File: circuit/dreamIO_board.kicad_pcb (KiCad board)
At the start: 2 copper layers, 60 x 60 mm, 82 parts, among them IC1 TPS61200, P1 BATT, P2 CONN_01X08, P3 CONN_01X08, P4 CONN_01X02, P5 CONN_01X06, P6 gnd_con, P7 CONN_01X03, P8 NO_CASCADE, P9 PixelOut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

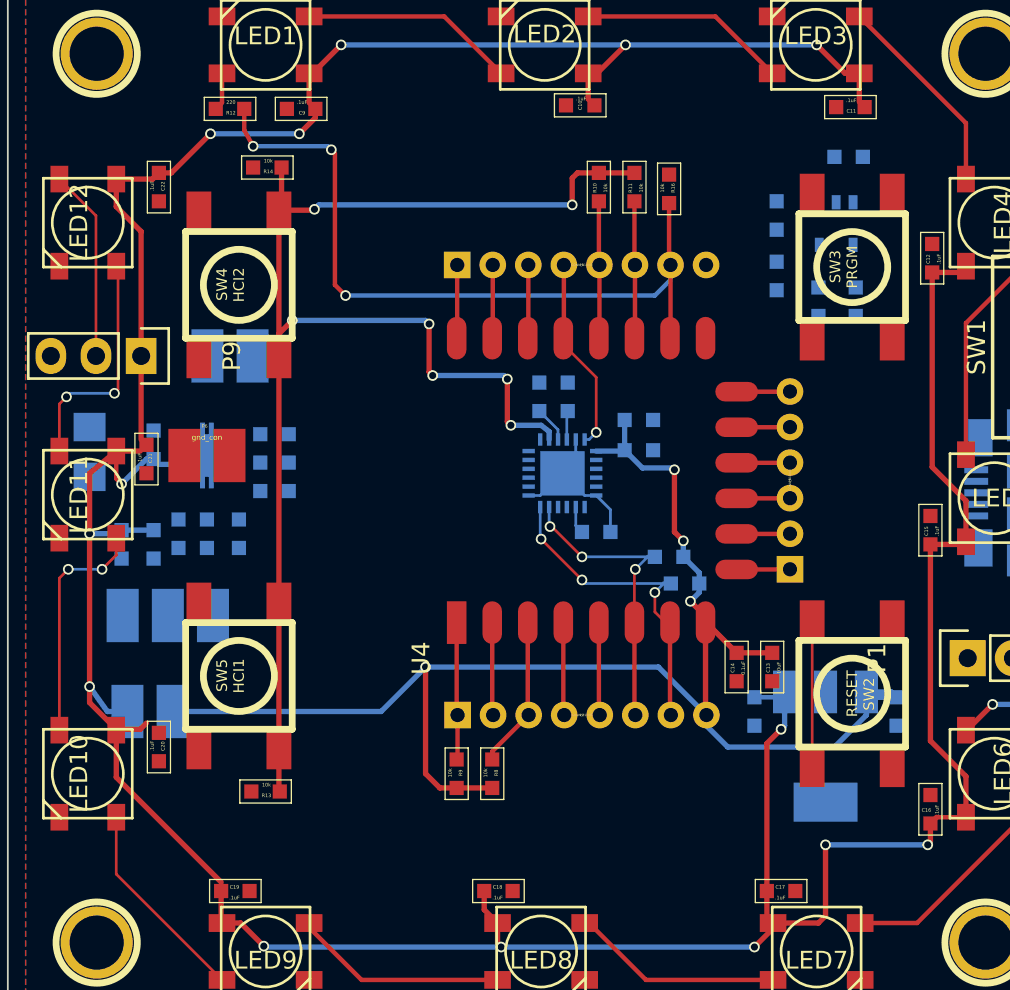
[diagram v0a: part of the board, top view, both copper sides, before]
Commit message: removed the 3.3V regulator. The TPS61200 is now the main regulator and will be 5V.
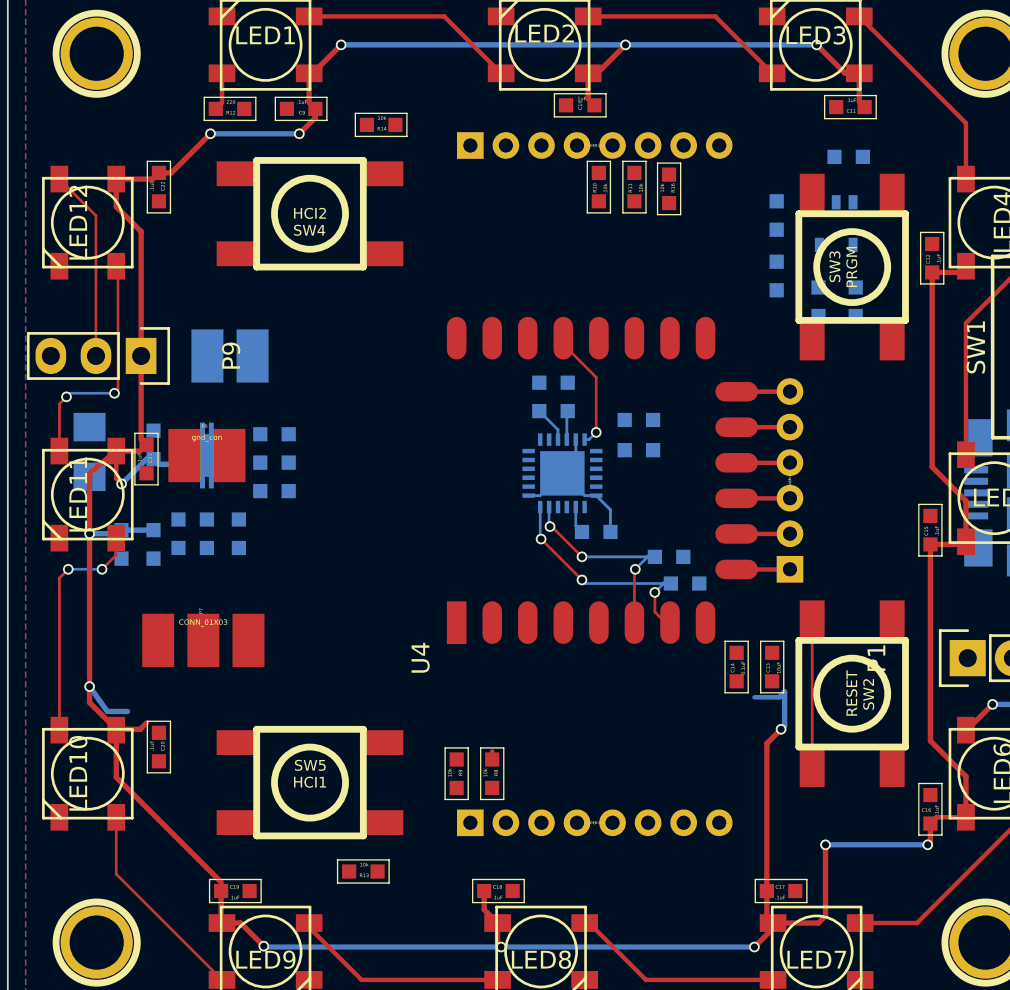
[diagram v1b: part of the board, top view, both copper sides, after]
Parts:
- removed C7: .33uF, kicad-libraries:0603
- removed C8: .1uF, kicad-libraries:0603
- removed P8: NO_CASCADE, _connectors:_Solder_Pad2.54_2
- removed U3: UA78M33_SOT223, kicad-libraries:SOT-223
- P7: moved to F.Cu
- moved SW5 7.21 mm to (31.3, 59.7), turned to 0 degrees
- moved R13 7.11 mm to (34.3, 64.7)
- moved R14 6.84 mm to (35.3, 22.7)
- moved P3 6.76 mm to (47.3, 23.9)
- moved P2 6.10 mm to (47.3, 62.0)
- moved SW4 5.66 mm to (31.3, 27.7), turned to 180 degrees
- moved P7 2.44 mm to (25.3, 51.7)
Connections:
- C10 pad 2: VCC -> +3V3
- C11 pad 2: VCC -> +3V3
- C12 pad 2: VCC -> +3V3
- C15 pad 2: VCC -> +3V3
- C16 pad 2: VCC -> +3V3
- C17 pad 2: VCC -> +3V3
- C18 pad 2: VCC -> +3V3
- C19 pad 2: VCC -> +3V3
- C20 pad 2: VCC -> +3V3
- C21 pad 2: VCC -> +3V3
- C22 pad 2: VCC -> +3V3
- C5 pad 1: VCC -> +3V3
- C9 pad 2: VCC -> +3V3
- IC1 pad 2: VCC -> +3V3
- LED1 pad 1: VCC -> +3V3
- LED10 pad 1: VCC -> +3V3
- LED11 pad 1: VCC -> +3V3
- LED12 pad 1: VCC -> +3V3
- LED2 pad 1: VCC -> +3V3
- LED3 pad 1: VCC -> +3V3
- LED4 pad 1: VCC -> +3V3
- LED5 pad 1: VCC -> +3V3
- LED6 pad 1: VCC -> +3V3
- LED7 pad 1: VCC -> +3V3
- LED8 pad 1: VCC -> +3V3
- LED9 pad 1: VCC -> +3V3
- P9 pad 1: VCC -> (no net)
- R4 pad 1: VCC -> +3V3
- R5 pad 1: VCC -> +3V3
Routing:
- net VCC: track 220.3 -> 0.00 mm, vias 14 -> 0
- net +3V3: track 164.3 -> 220.3 mm, vias 11 -> 14
- net GPIO15: track 42.4 -> 0.04 mm, vias 3 -> 0
- net CH_PD: track 8.57 -> 0.45 mm
- net GPIO2: track 7.72 -> 0.04 mm
- net GPIO0: track 7.72 -> 0.04 mm
- net RESET: track 16.1 -> 8.47 mm
- net GPIO13: track 18.7 -> 13.5 mm
- net GPIO12: track 17.4 -> 12.1 mm
- net GPIO16: track 5.22 -> 0.00 mm
- net GPIO14: track 5.22 -> 0.00 mm
- net ADC: track 5.22 -> 0.00 mm
- net GPIO4: track 11.0 -> 6.92 mm
- net TX: track 4.13 -> 0.04 mm
- net RX: track 4.13 -> 0.04 mm
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
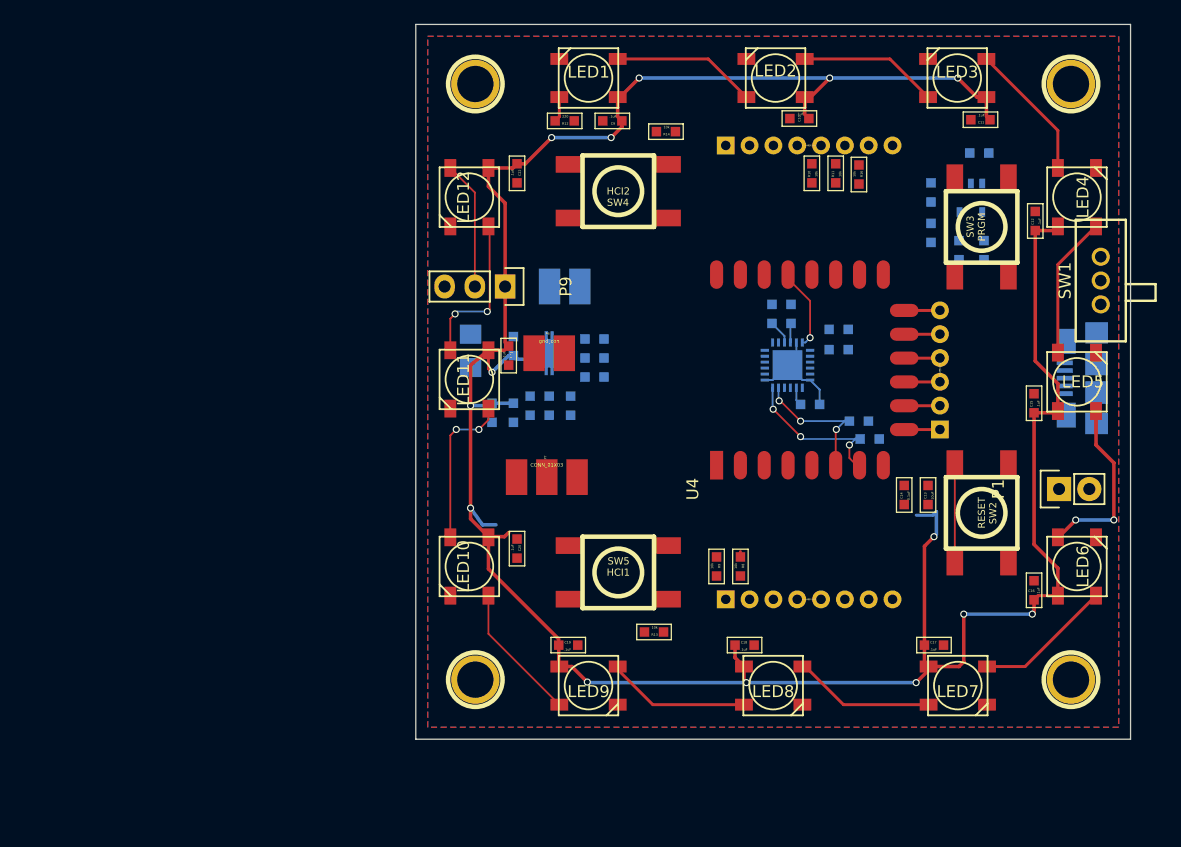
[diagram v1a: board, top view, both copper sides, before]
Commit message: added ADC voltage measurement. A voltage resistor of R1 2M and R2 330K keeps the maximum voltage of the battery (4.2V) below the 1V maximum for the analog pin. If the resistor network is not populated the pin remains empty
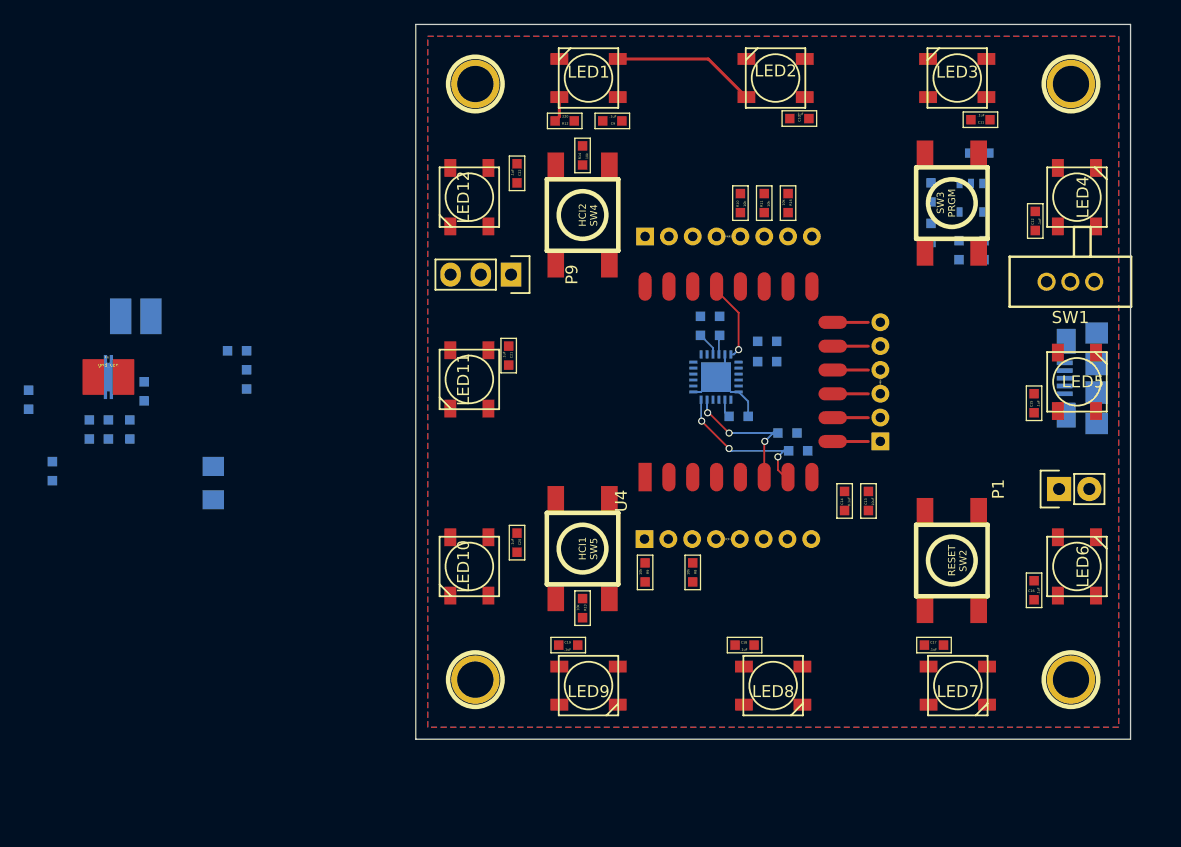
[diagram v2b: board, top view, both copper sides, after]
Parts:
- removed P7: CONN_01X03, _connectors:_Solder_Pad2.54_3
- removed R5: 2M, kicad-libraries:0603
- moved C5 40.9 mm to (-18.2, 45.2)
- moved R4 39.0 mm to (-16.2, 51.2)
- moved C3 37.1 mm to (-8.50, 44.5)
- moved C6 37.1 mm to (-13.1, 47.7)
- moved IC1 37.1 mm to (-11.5, 43.3)
- moved P6 37.1 mm to (-11.5, 43.3)
- moved R6 37.1 mm to (-11.5, 47.7)
- moved R7 37.1 mm to (-9.70, 47.7)
- moved P4 36.1 mm to (-9.20, 38.2)
- moved C4 30.0 mm to (0.10, 43.5)
- moved R3 30.0 mm to (-0.70, 41.1)
- moved L1 24.3 mm to (-2.70, 52.2)
- moved P3 10.2 mm to (40.5, 31.5)
- moved P2 8.49 mm to (40.5, 56.9)
- moved R14 7.28 mm to (28.3, 24.7), turned to 270 degrees
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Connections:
- R4 pad 2: Net-(P7-Pad3) -> Net-(IC1-Pad10)
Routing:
- net +3V3: track 220.3 -> 0.00 mm, vias 14 -> 0
- net Net-(LED5-Pad2): track 15.1 -> 0.05 mm, vias 2 -> 0
- net Net-(LED11-Pad2): track 13.3 -> 0.00 mm, vias 2 -> 0
- net Net-(LED10-Pad2): track 13.2 -> 0.00 mm, vias 2 -> 0
- net Net-(LED8-Pad2): track 12.1 -> 0.00 mm
- net Net-(LED7-Pad2): track 11.9 -> 0.00 mm
- net Net-(LED4-Pad2): track 11.9 -> 0.00 mm
- net Net-(LED2-Pad2): track 11.7 -> 0.00 mm
- net Net-(LED3-Pad2): track 11.6 -> 0.00 mm
- net Net-(LED6-Pad2): track 11.6 -> 0.00 mm
- net Net-(LED10-Pad4): track 11.6 -> 0.00 mm
- net DOUT: track 10.8 -> 0.00 mm
- net RESET: track 8.47 -> 0.00 mm

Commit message: changed position of on-off switch, batt connection, and USB input. Realized the USB plug didn`t have to be right in the center of one side
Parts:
- added R15: 330K, kicad-libraries:0603, F.Cu at (21.7, 79.3)
- added R5: 2M, kicad-libraries:0603, F.Cu at (23.3, 79.3)
- moved R4 79.3 mm to (63.1, 49.3), turned to 90 degrees
- moved R6 76.7 mm to (65.2, 47.7), turned to 180 degrees
- moved C5 75.6 mm to (57.4, 47.3), turned to 180 degrees
- moved IC1 73.0 mm to (61.5, 45.6)
- moved P6 73.0 mm to (61.5, 45.6), turned to 180 degrees
- moved C6 70.5 mm to (57.4, 48.8), turned to 180 degrees
- moved C3 68.4 mm to (59.9, 42.1), turned to 0 degrees
- moved P4 68.3 mm to (59.1, 39.1)
- moved R7 67.2 mm to (57.4, 50.3), turned to 180 degrees
- moved R3 66.1 mm to (65.2, 46.4), turned to 0 degrees
- moved C4 65.1 mm to (65.2, 44.8), turned to 180 degrees
- moved L1 60.4 mm to (57.1, 43.9), turned to 90 degrees
- moved SW1 18.2 mm to (68.1, 53.5)
- moved P1 3.06 mm to (68.9, 49.7)
- moved U2 2.31 mm to (73.1, 41.1)
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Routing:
- net RESET: track 0.00 -> 7.24 mm
- net CH_PD: track 0.00 -> 7.24 mm
- net GPIO2: track 0.04 -> 6.24 mm
- net GPIO15: track 0.04 -> 6.24 mm
- net GPIO0: track 0.04 -> 6.24 mm
- net GPIO16: track 0.00 -> 5.22 mm
- net GPIO14: track 0.00 -> 5.22 mm
- net GPIO13: track 13.5 -> 18.7 mm
- net ADC: track 0.00 -> 5.22 mm
- net +3V3: track 0.00 -> 5.22 mm
- net GPIO12: track 12.1 -> 17.4 mm
- net GPIO4: track 6.92 -> 11.1 mm
- net TX: track 0.04 -> 4.24 mm
- net RX: track 0.04 -> 4.24 mm
- net GPIO5: track 0.04 -> 4.24 mm
- added copper zone on B.Cu, net GNDA
- added copper zone on F.Cu, net GNDA

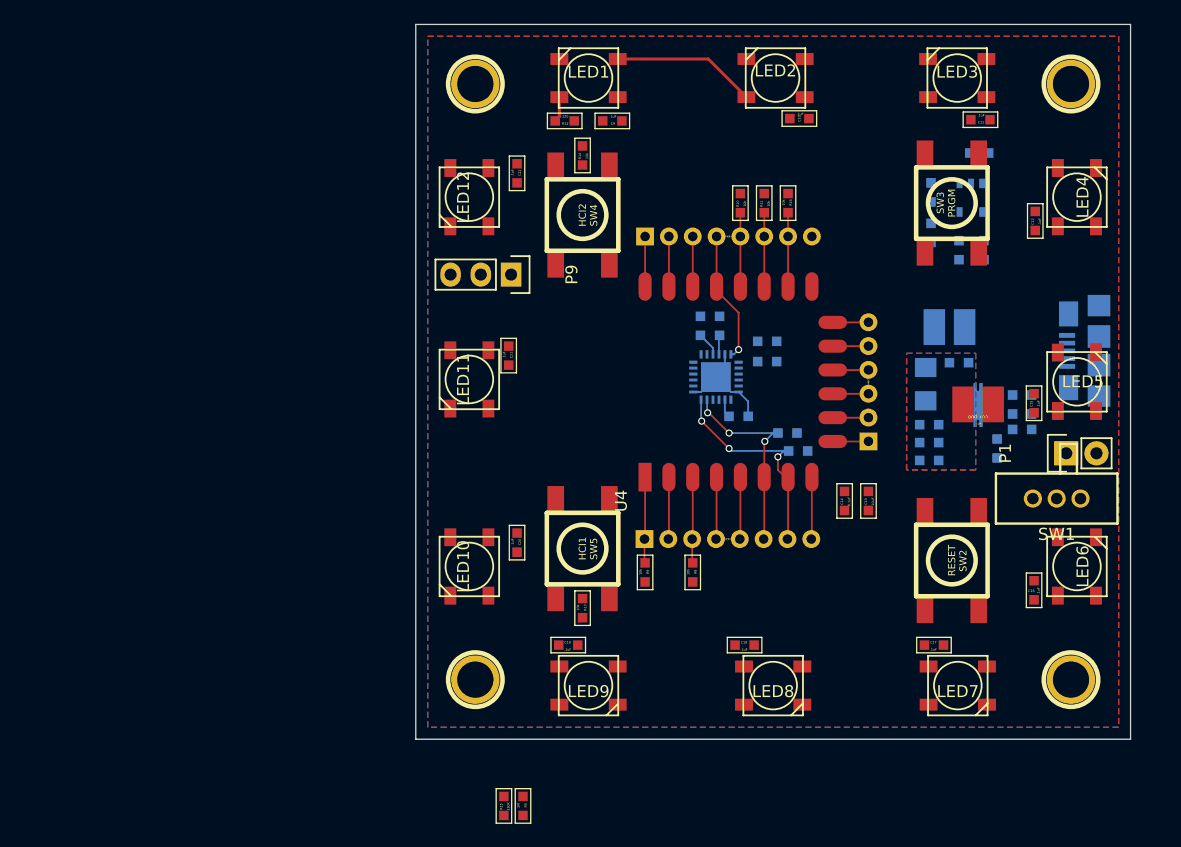
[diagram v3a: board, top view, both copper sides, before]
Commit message: laid a few more traces. roughly 78 to go;
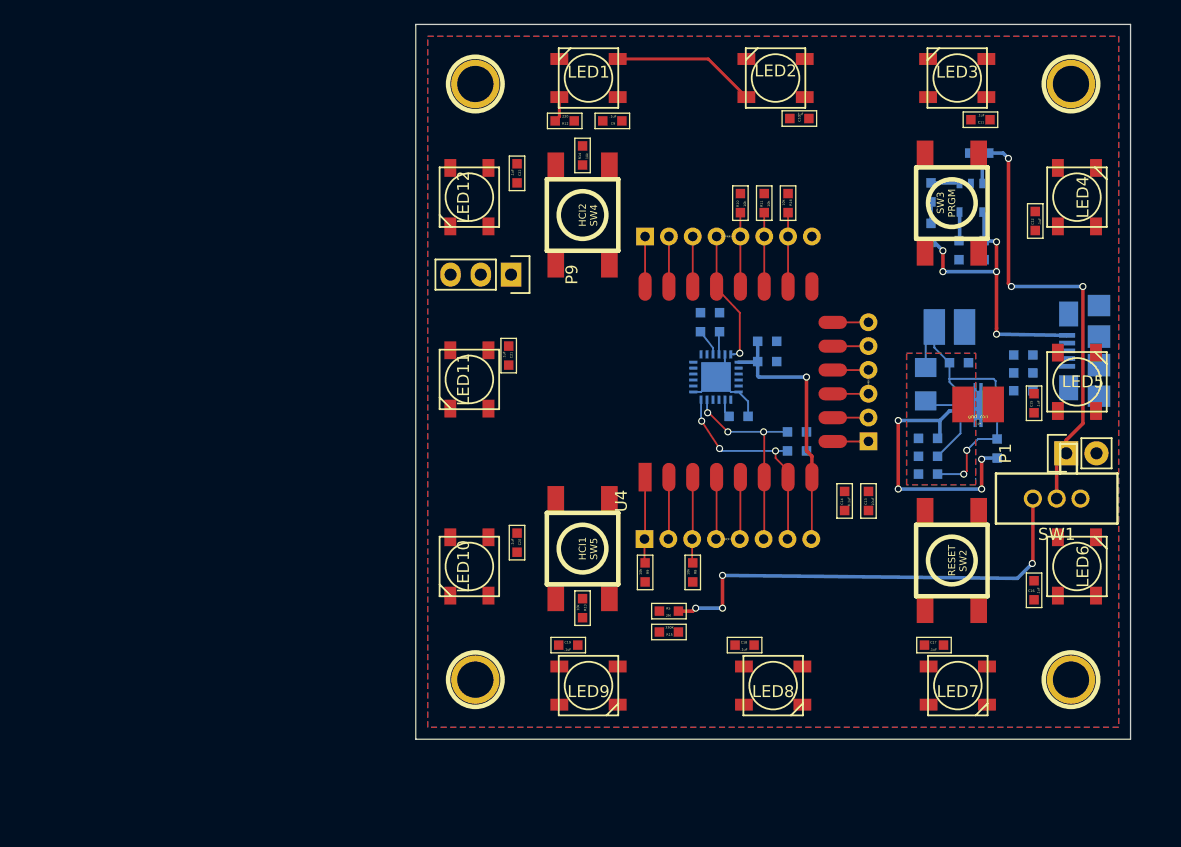
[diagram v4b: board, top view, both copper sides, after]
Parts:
- moved R5 20.4 mm to (35.5, 63.0), turned to 180 degrees
- moved R15 20.1 mm to (35.5, 64.7), turned to 0 degrees
- moved R6 6.25 mm to (65.3, 41.5)
- moved R3 3.45 mm to (65.3, 43.0)
- moved C5 1.15 mm to (57.3, 48.5)
- moved C6 1.15 mm to (57.3, 50.0)
- moved R7 1.15 mm to (57.3, 51.5)
- moved R25 0.81 mm to (46.3, 47.9)
- moved C4 0.36 mm to (65.3, 44.5)
- moved C25 0.30 mm to (39.8, 38.7)
- moved R27 0.30 mm to (38.2, 38.7)
- moved R26 0.10 mm to (46.3, 49.5)
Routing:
- net Net-(C3-Pad1): track 0.00 -> 54.0 mm, vias 0 -> 4
- net +3V3: track 5.22 -> 46.2 mm, vias 0 -> 5
- net +BATT: track 0.00 -> 40.2 mm, vias 0 -> 3
- net /VIN: track 0.00 -> 24.8 mm, vias 0 -> 5
- net Net-(IC1-Pad10): track 0.00 -> 9.15 mm, vias 0 -> 2
- net Net-(C6-Pad1): track 0.00 -> 4.10 mm
- net Net-(IC1-Pad3): track 0.00 -> 3.07 mm
- net Net-(R2-Pad1): track 0.00 -> 2.42 mm
- net Net-(D1-Pad1): track 0.00 -> 2.42 mm
- net Net-(D1-Pad2): track 0.00 -> 1.80 mm
- net Net-(C4-Pad2): track 0.00 -> 0.67 mm
